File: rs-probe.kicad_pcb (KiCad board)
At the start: 4 copper layers, 40 x 14 mm, 108 parts, among them J1 USB_C_Receptacle_USB2.0, J10 Conn_01x01, J11 Conn_01x01, J2 Castellated Vias, J3 Castellated Vias, J4 Castellated Vias, J5 tag-connect-swd, J6 Conn_01x01, J7 Conn_01x01, J8 Conn_01x01, J9 Conn_01x01, Q1 NTZD3155C or CMLDM3757-TR-PBF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, SW1 EVQ-P2002W, T1 Tab, T2 Tab, U1 74LVC1T45GM,115, U10 74LVC1T45GM,115, U11 74LVC1T45GM,115, U12 NCP133AMXADJTCG, U13 NCP133AMXADJTCG, U14 NCP133AMXADJTCG, U2 74LVC1T45GM,115, U3 W25Q8, U4 NUF8401MNT4G, U5 CortexDebug, U6 RP2040, U7 NUF2042XV6T1G, U8 74LVC1T45GM,115, U9 74LVC1T45GM,115, X1 12 MHz

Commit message: Lots of work
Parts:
- removed J10, J11: Conn_01x01, connectors:pad_1.5x2.0mm
- removed J4: Castellated Vias, connectors:1x3_1.5mm_castellated
- removed TP1, TP2, TP3, TP4: TestPoint, TestPoint:TestPoint_Pad_D1.0mm
- added C31: 0.1u, passive:C_0402, F.Cu at (163.7, 90.3)
- added C32: 0.1u, passive:C_0402, F.Cu at (163.7, 87.1)
- added C33: 0.1u, passive:C_0402, F.Cu at (163.7, 88.7)
- added C34: 0.1u, passive:C_0402, F.Cu at (163.7, 83.1)
- added C35: 0.1u, passive:C_0402, F.Cu at (163.7, 84.7)
- added J1: Conn_01x01, connectors:pad_2.0x2.5mm, F.Cu at (149.9, 91.4)
- added J5: Conn_01x01, connectors:pad_2.0x2.5mm, B.Cu at (157.0, 107.0)
- J2: value Castellated Vias -> Conn_01x01; footprint connectors:1x9_1.5mm_castellated -> connectors:pad_2.0x2.5mm; moved to F.Cu
- J3: value Castellated Vias -> Conn_01x01; footprint connectors:1x2_1.5mm_castellated -> connectors:pad_2.0x2.5mm; moved to F.Cu
- J6, J7, J8, J9: footprint connectors:pad_1.5x2.0mm -> connectors:pad_2.0x2.5mm
- R10, R18, R22, R23, R24, R26: value 1Meg -> 1M
- X1: renamed from U5; value CortexDebug -> Conn_ST_STDC14
- X5: renamed from J5; value tag-connect-swd -> TagConnect
- moved J3 25.9 mm to (156.1, 91.4), turned to 0 degrees
- moved J7 22.7 mm to (166.0, 110.5)
- moved R19 21.5 mm to (173.3, 82.4), turned to 0 degrees
- moved R20 21.3 mm to (175.1, 81.8), turned to 90 degrees
- moved Q1 20.1 mm to (173.8, 81.0), turned to 90 degrees
- moved J8 19.3 mm to (163.0, 110.5)
- moved J9 19.2 mm to (160.0, 110.5)
- moved X5 17.6 mm to (169.9, 75.6)
- moved C25 16.5 mm to (165.1, 67.2)
- moved J6 15.6 mm to (154.0, 107.0)
- moved C5 14.0 mm to (158.8, 80.3), turned to 180 degrees
- moved R21 13.7 mm to (164.7, 68.6)
- moved R25 13.7 mm to (165.6, 68.6), turned to 90 degrees
- moved U12 13.7 mm to (163.2, 68.5)
- moved C24 13.7 mm to (163.2, 67.1)
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- renumbered J1 to X10, X1 to XC1
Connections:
- net /5V_KEY_EN renamed 5V_KEY_EN
- net /ADJ2_T renamed ADJ2_T
- net /ADJ_T renamed ADJ_T
- net /DIR_SWDCLK_JCLK renamed DIR_SWDCLK_JCLK
- net /DIR_SWDIO_TMS renamed DIR_SWDIO_TMS
- net /DIR_SWO_TDO renamed DIR_SWO_TDO
- net /DIR_TDI renamed DIR_TDI
- net /DIR_VCP_RX renamed DIR_VCP_RX
- net /DIR_VCP_TX renamed DIR_VCP_TX
- net /D_FS_N renamed D_FS_N
- net /D_FS_P renamed D_FS_P
- net /FUSED_5V renamed FUSED_5V
- net /GNDDetect renamed GNDDetect
- net /LED1 renamed LED1
- net /LED2 renamed LED2
- net /LED3 renamed LED3
- net /PROTECTED_5V renamed PROTECTED_5V
- net /PWM2_VS renamed PWM2_VS
- net /PWM_VS renamed PWM_VS
- net /P_SWCLK renamed P_SWCLK
- net /P_SWDIO renamed P_SWDIO
- net /SWDCLK_JCLK renamed SWDCLK_JCLK
- net /SWDIO_TMS renamed SWDIO_TMS
- net /SWO_TDO renamed SWO_TDO
- net /TDI renamed TDI
- net /TRANS_VCC renamed TRANS_VCC
- net /T_VCC_EN renamed T_VCC_EN
- net /T_VCC_MEAS renamed T_VCC_MEAS
- net /VCP_RX renamed VCP_RX
- net /VCP_TX renamed VCP_TX
- net /VS2_T renamed VS2_T
- net /VS_T renamed VS_T
- net /~{RESET} renamed ~{RESET}
- C27 pad 1: /T_VCC -> T_VCC
- D3 pad 1: /T_VCC -> T_VCC
- J2 pad 1: GND -> T_VCP_TX
- J3 pad 1: /5V_KEY -> T_VCP_RX
- J6 pad 1: GND -> 5V_KEY
- J7 pad 1: /T_VCC -> GPIO2
- J8 pad 1: /T_SWDIO_TMS -> T_VCC
- J9 pad 1: /T_SWDCLK_JCLK -> GPIO1
- Q1 pad 3: /5V_KEY -> 5V_KEY
- R10 pad 2: /T_TDI -> T_TDI
- R14 pad 2: /T_VCC -> T_VCC
- R18 pad 2: /T_VCP_RX -> T_VCP_RX
- R22 pad 2: /T_SWDIO_TMS -> T_SWDIO_TMS
- R23 pad 2: /T_SWDCLK_JCLK -> T_SWDCLK_JCLK
- R24 pad 2: /T_SWO_TDO -> T_SWO_TDO
- R26 pad 2: /T_VCP_TX -> T_VCP_TX
- R9 pad 1: /T_VCC -> T_VCC
- U4 pad 10: /T_SWDCLK_JCLK -> T_SWDCLK_JCLK
- U4 pad 11: /T_SWO_TDO -> T_SWO_TDO
- U4 pad 12: /T_TDI -> T_TDI
- U4 pad 13: /T_GNDDetect -> T_GNDDetect
- U4 pad 14: /T_~{RESET} -> T_~{RESET}
- U4 pad 15: /T_VCP_TX -> T_VCP_TX
- U4 pad 16: /T_VCP_RX -> T_VCP_RX
- U4 pad 9: /T_SWDIO_TMS -> T_SWDIO_TMS
- U6 pad 3: /GPIO1 -> GPIO1
- U6 pad 4: /GPIO2 -> GPIO2
- X1 pad 1: /T_VCC -> T_VCC
- X1 pad 10: /T_~{RESET} -> T_~{RESET}
- X1 pad 2: /T_SWDIO_TMS -> T_SWDIO_TMS
- X1 pad 4: /T_SWDCLK_JCLK -> T_SWDCLK_JCLK
- X1 pad 6: /T_SWO_TDO -> T_SWO_TDO
- X1 pad 7: /5V_KEY -> unconnected-(X1-KEY-Pad7)
- X1 pad 8: /T_TDI -> T_TDI
- X1 pad 9: /T_GNDDetect -> T_GNDDetect
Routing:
- net GND: track 99.8 -> 34.3 mm, vias 63 -> 33
- net /5V_KEY: track 51.8 -> 0.00 mm, vias 3 -> 0
- net /T_VCC: track 50.3 -> 0.00 mm, vias 4 -> 0
- net +3.3V: track 58.5 -> 21.8 mm, vias 18 -> 15
- net P_SWDIO: track 29.7 -> 0.00 mm, vias 1 -> 0
- net P_SWCLK: track 28.2 -> 0.00 mm, vias 1 -> 0
- net T_VCC_MEAS: track 27.3 -> 2.11 mm, vias 2 -> 0
- net /T_SWDIO_TMS: track 23.6 -> 0.00 mm, vias 3 -> 0
- net 5V_KEY_EN: track 24.0 -> 0.70 mm, vias 2 -> 0
- net /T_VCP_RX: track 22.0 -> 0.00 mm, vias 4 -> 0
- net /T_SWDCLK_JCLK: track 21.1 -> 0.00 mm, vias 3 -> 0
- net VS2_T: track 22.7 -> 1.60 mm, vias 2 -> 0
- net VS_T: track 19.0 -> 1.60 mm, vias 2 -> 0
- net /T_VCP_TX: track 17.3 -> 0.00 mm, vias 3 -> 0
- net /T_GNDDetect: track 16.1 -> 0.00 mm, vias 1 -> 0
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- added copper zone on B.Cu, net +3.3V
- added copper zone on F.Cu, net +3.3V
- removed copper zone on B.Cu, net GND
- removed copper zone on F.Cu, net GND

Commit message: wip
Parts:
- moved J7 35.8 mm to (154.8, 76.5)
- moved J8 35.8 mm to (151.8, 76.5)
- moved J9 35.8 mm to (148.8, 76.5)
- moved C24 16.9 mm to (171.1, 82.1)
- moved J5 16.8 mm to (150.8, 91.4), turned to 0 degrees
- moved J6 15.6 mm to (153.8, 91.4), turned to 0 degrees
- moved C25 15.5 mm to (169.4, 82.1), turned to 180 degrees
- moved U12 14.7 mm to (171.1, 80.8)
- moved R21 13.3 mm to (169.8, 80.8)
- moved R25 12.7 mm to (169.0, 80.8)
- moved X5 6.11 mm to (163.9, 76.8)
- moved R5 1.70 mm to (175.5, 92.2)
- moved R6 1.65 mm to (173.8, 92.2)
- moved C6 1.10 mm to (176.8, 90.8)
- moved R7 0.81 mm to (177.1, 92.2)
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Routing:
- net T_VCC_MEAS: track 2.11 -> 30.5 mm, vias 0 -> 2
- net DIR_VCP_TX: track 0.00 -> 14.0 mm, vias 0 -> 2
- net DIR_VCP_RX: track 0.00 -> 12.3 mm, vias 0 -> 2
- net TRANS_VCC: track 19.2 -> 7.76 mm
- net DIR_SWDCLK_JCLK: track 0.00 -> 11.0 mm, vias 0 -> 3
- net VCP_RX: track 0.00 -> 11.0 mm, vias 0 -> 2
- net VCP_TX: track 0.00 -> 10.5 mm, vias 0 -> 2
- net SWDIO_TMS: track 0.00 -> 9.68 mm, vias 0 -> 2
- net SWO_TDO: track 0.00 -> 8.99 mm, vias 0 -> 2
- net SWDCLK_JCLK: track 0.00 -> 8.58 mm, vias 0 -> 2
- net TDI: track 0.00 -> 8.56 mm, vias 0 -> 2
- net DIR_TDI: track 0.00 -> 5.48 mm, vias 0 -> 1
- net GND: track 34.3 -> 37.8 mm, vias 33 -> 36
- net Net-(D1-RK): track 2.46 -> 4.96 mm, vias 0 -> 2
- net +3.3V: track 21.8 -> 24.2 mm
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- added copper zone on B.Cu, net GND
- added copper zone on F.Cu, net GND
- removed copper zone on B.Cu, net +3.3V
- removed copper zone on F.Cu, net +3.3V

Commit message: wip
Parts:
- removed X5: TagConnect, Connector:Tag-Connect_TC2030-IDC-NL_2x03_P1.27mm_Vertical
- removed kibuzzard-61EE8014: G***, kibuzzard-61EE8014
- removed kibuzzard-61FE7ECB: G***, kibuzzard-61FE7ECB
- removed kibuzzard-61FE8065: G***, kibuzzard-61FE8065
- removed kibuzzard-61FE8092: G***, kibuzzard-61FE8092
- removed kibuzzard-61FE80B0: G***, kibuzzard-61FE80B0
- removed kibuzzard-61FE80BD: G***, kibuzzard-61FE80BD
- removed kibuzzard-6228D4B3: G***, kibuzzard-6228D4B3
- removed kibuzzard-6228D4CF: G***, kibuzzard-6228D4CF
- removed kibuzzard-63846A4C: G***, kibuzzard-63846A4C
- removed kibuzzard-6384B72D: G***, kibuzzard-6384B72D
- moved SW1 28.8 mm to (162.2, 96.9)
- moved J6 10.5 mm to (152.4, 81.0)
- moved J5 10.3 mm to (150.1, 81.1)
- moved F1 8.49 mm to (186.9, 79.9)
- moved C17 6.80 mm to (156.9, 91.0), turned to 180 degrees
- moved C19 6.79 mm to (156.9, 91.8), turned to 180 degrees
- moved FB1 6.58 mm to (183.0, 79.9), turned to 180 degrees
- moved C29 6.34 mm to (184.6, 79.9), turned to 180 degrees
- moved C16 5.20 mm to (158.6, 82.9), turned to 180 degrees
- moved C34 5.15 mm to (158.6, 83.8), turned to 180 degrees
- moved D2 5.04 mm to (181.2, 79.9)
- moved U12 4.55 mm to (175.6, 80.1)
- moved C24 4.55 mm to (175.6, 81.4)
- moved C25 4.55 mm to (173.9, 81.4)
- moved R21 4.55 mm to (174.3, 80.2)
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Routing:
- net GNDDetect: track 13.9 -> 1.20 mm
- net ~{RESET}: track 13.0 -> 1.18 mm
- net DIR_VCP_RX: track 12.3 -> 0.92 mm
- net DIR_VCP_TX: track 14.0 -> 2.92 mm
- net DIR_SWDCLK_JCLK: track 11.0 -> 1.04 mm, vias 3 -> 1
- net VCP_RX: track 11.0 -> 1.18 mm
- net SWDIO_TMS: track 9.68 -> 0.56 mm
- net SWO_TDO: track 8.99 -> 0.00 mm, vias 2 -> 0
- net SWDCLK_JCLK: track 8.58 -> 0.26 mm, vias 2 -> 1
- net TDI: track 8.56 -> 0.31 mm, vias 2 -> 1
- net VCP_TX: track 10.5 -> 3.72 mm
- net +5V: track 4.29 -> 9.82 mm, vias 3 -> 2
- net Net-(U3-DO(IO1)): track 0.00 -> 4.62 mm, vias 0 -> 2
- net P_SWCLK: track 1.12 -> 4.94 mm
- net +3.3V: track 24.2 -> 27.9 mm
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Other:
- board text removed: "By Emil Fresk @korken89"
- board text removed: "git: {GITHASH}"

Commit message: wip
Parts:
- moved SW1 21.2 mm to (169.6, 77.0)
- moved R9 11.9 mm to (159.9, 89.8), turned to -90 degrees
- moved R11 11.7 mm to (159.4, 91.5), turned to 180 degrees
- moved J6 7.48 mm to (145.1, 79.5)
- moved R12 6.15 mm to (157.4, 82.0)
- moved C21 5.66 mm to (156.2, 81.8), turned to 90 degrees
- moved R27 5.62 mm to (159.2, 82.0), turned to 0 degrees
- moved C28 5.25 mm to (161.2, 81.6)
- moved R29 5.20 mm to (160.4, 81.6)
- moved J5 5.17 mm to (145.1, 82.2)
- moved C27 4.52 mm to (149.5, 80.8)
- moved C5 4.52 mm to (154.1, 80.4)
- moved D3 4.52 mm to (150.7, 82.2)
- moved R1 4.52 mm to (155.7, 80.4)
- moved R14 4.52 mm to (152.4, 82.2)
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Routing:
- net GND: track 41.5 -> 20.1 mm, vias 38 -> 42
- net T_VCC_MEAS: track 32.4 -> 14.1 mm, vias 2 -> 3
- net TRANS_VCC: track 11.2 -> 4.64 mm
- net T_VCC: track 10.0 -> 4.58 mm
- net 5V_KEY_EN: track 5.92 -> 0.84 mm
- net Net-(U1-B): track 3.61 -> 0.00 mm
- net +3.3V: track 27.9 -> 24.5 mm
- net VCP_TX: track 3.72 -> 0.64 mm
- net T_VCP_RX: track 8.15 -> 5.18 mm
- net DIR_TDI: track 2.59 -> 0.00 mm
- net Net-(U2-B): track 2.16 -> 0.00 mm
- net DIR_VCP_TX: track 2.92 -> 0.90 mm
- net ADJ2_T: track 3.17 -> 1.31 mm
- net VS2_T: track 1.60 -> 0.00 mm
- net Net-(D1-RK): track 4.96 -> 3.59 mm
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
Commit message: wip
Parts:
- added X5: TagConnect, Connector:Tag-Connect_TC2030-IDC-NL_2x03_P1.27mm_Vertical, F.Cu at (166.5, 75.4)
- SW1: footprint Button_Switch_SMD:SW_SPST_EVQP2 -> pushbuttons:PCB_JumperButton; moved to B.Cu
- moved SW1 18.3 mm to (186.6, 84.0), turned to 180 degrees
- moved R9 3.56 mm to (156.9, 91.8), turned to 0 degrees
- moved C19 3.28 mm to (159.7, 90.0), turned to 90 degrees
- moved R11 1.33 mm to (158.2, 91.8), turned to 90 degrees
- moved C20 0.32 mm to (163.4, 88.8)
- moved C31 0.32 mm to (163.4, 89.6)
- moved C18 0.16 mm to (163.4, 87.0)
- moved C33 0.16 mm to (163.4, 87.8)
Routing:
- net T_VCC: track 4.58 -> 19.0 mm, vias 0 -> 2
- net VCP_RX: track 1.28 -> 14.3 mm
- net VCP_TX: track 0.64 -> 11.8 mm
- net Net-(R2-Pad2): track 0.00 -> 8.02 mm, vias 0 -> 1
- net DIR_SWDCLK_JCLK: track 1.04 -> 6.89 mm, vias 1 -> 2
- net GND: track 20.1 -> 25.0 mm
- net SWDCLK_JCLK: track 0.26 -> 4.99 mm, vias 1 -> 2
- net DIR_VCP_RX: track 0.61 -> 5.26 mm
- net TDI: track 0.00 -> 4.21 mm
- net P_SWCLK: track 4.31 -> 0.44 mm, vias 1 -> 0
- net T_VCC_MEAS: track 14.1 -> 17.8 mm, vias 3 -> 0
- net +3.3V: track 24.5 -> 20.8 mm
- net TRANS_VCC: track 4.64 -> 8.03 mm, vias 5 -> 8
- net DIR_TDI: track 0.00 -> 2.84 mm
- net P_SWDIO: track 2.93 -> 0.32 mm, vias 1 -> 0
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- removed copper zone on In2.Cu, net GND

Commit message: wip
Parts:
- removed X5: TagConnect, Connector:Tag-Connect_TC2030-IDC-NL_2x03_P1.27mm_Vertical
- J5, J6, J7, J8, J9: moved to F.Cu
- moved J6 28.5 mm to (173.6, 80.5), turned to 180 degrees
- moved J9 20.4 mm to (168.8, 80.5), turned to 0 degrees
- moved J8 19.8 mm to (171.2, 80.5), turned to 0 degrees
- moved J5 19.0 mm to (164.0, 80.5), turned to 180 degrees
- moved J7 12.3 mm to (166.4, 80.5), turned to 0 degrees
- moved R25 3.56 mm to (175.5, 83.1), turned to 0 degrees
- moved C25 2.55 mm to (176.4, 81.9), turned to -90 degrees
- moved C24 2.19 mm to (177.7, 81.9), turned to -90 degrees
- moved R21 2.18 mm to (175.6, 81.9), turned to 90 degrees
- moved U12 0.88 mm to (176.5, 80.2)
- moved R28 0.54 mm to (162.1, 80.8), turned to -90 degrees
- moved R17 0.21 mm to (166.9, 83.1)
- moved R4 0.20 mm to (185.1, 91.8)
- moved J2 0.20 mm to (152.4, 91.5)
- moved J1 0.20 mm to (149.9, 91.6)
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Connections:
- U6 pad 11: GNDDetect -> unconnected-(U6-GPIO8-Pad11)
- U6 pad 12: ~{RESET} -> unconnected-(U6-GPIO9-Pad12)
- U6 pad 16: unconnected-(U6-GPIO13-Pad16) -> DIR_SWDCLK_JCLK
- U6 pad 17: unconnected-(U6-GPIO14-Pad17) -> GNDDetect
- U6 pad 18: unconnected-(U6-GPIO15-Pad18) -> ~{RESET}
- U6 pad 29: unconnected-(U6-GPIO18-Pad29) -> DIR_TDI
- U6 pad 30: DIR_SWDCLK_JCLK -> DIR_VCP_TX
- U6 pad 35: DIR_TDI -> unconnected-(U6-GPIO23-Pad35)
- U6 pad 36: DIR_VCP_TX -> unconnected-(U6-GPIO24-Pad36)
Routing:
- net FUSED_5V: track 10.2 -> 80.3 mm, vias 0 -> 5
- net TRANS_VCC: track 8.03 -> 33.1 mm
- net T_VCC: track 19.0 -> 43.8 mm, vias 2 -> 3
- net T_VCC_EN: track 0.00 -> 24.0 mm
- net PWM_VS: track 0.00 -> 20.4 mm, vias 0 -> 2
- net ~{RESET}: track 0.64 -> 20.4 mm
- net GNDDetect: track 0.00 -> 18.8 mm, vias 1 -> 2
- net PWM2_VS: track 0.00 -> 11.6 mm, vias 0 -> 2
- net SWO_TDO: track 0.00 -> 11.4 mm, vias 1 -> 2
- net DIR_SWO_TDO: track 0.00 -> 11.3 mm, vias 1 -> 2
- net DIR_VCP_RX: track 5.26 -> 15.9 mm
- net DIR_SWDIO_TMS: track 0.00 -> 9.60 mm
- net SWDIO_TMS: track 0.56 -> 9.89 mm
- net GPIO2: track 0.00 -> 8.66 mm
- net +5V: track 8.77 -> 0.24 mm, vias 2 -> 4
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- added copper zone on F.Cu, net +3.3V
- added copper zone on In2.Cu, net +5V

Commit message: clearing drc errors
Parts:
- D1: value LTST-C19HE1WT -> 7
- U13, U14: footprint Package_DFN_QFN:DFN-6-1EP_1.2x1.2mm_P0.4mm_EP0.3x0.94mm_PullBack -> dfn:DFN-6-1EP_1.2x1.2mm_P0.4mm_EP0.3x0.94mm_PullBack
- moved J3 1.20 mm to (154.9, 91.5)

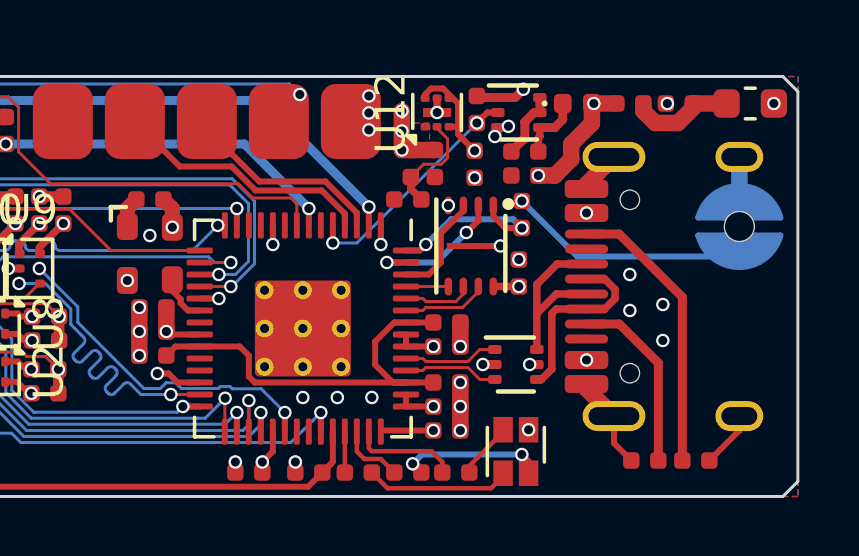
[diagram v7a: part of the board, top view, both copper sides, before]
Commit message: fixing missing 3D models
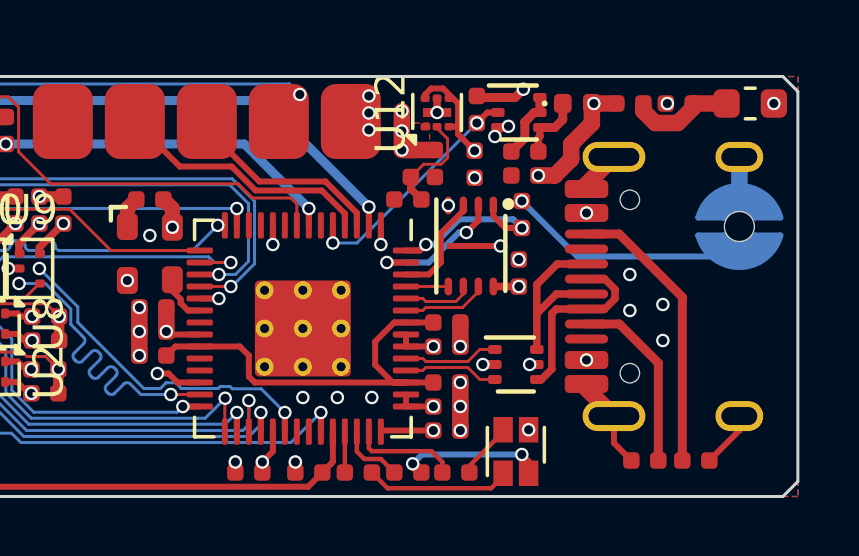
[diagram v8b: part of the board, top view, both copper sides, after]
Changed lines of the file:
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@@
 			(pintype "passive")
 		)
-		(model "${KICAD8_3DMODEL_DIR}/Diode_SMD.3dshapes/D_0402_1005Metric.wrl"
+		(model "${KIPRJMOD}/kicad_libs/3dmodels/step/SMD1006_step/3D_Model_SMD1006_Rev.0.stp"
 			(offset
 				(xyz 0 0 0)
@@
 			)
 			(rotate
-				(xyz 0 0 0)
+				(xyz 0 0 90)
 			)
 		)
@@
 			(pintype "passive")
 		)
-		(model "${KICAD8_3DMODEL_DIR}/LED_SMD.3dshapes/LED_LiteOn_LTST-C19HE1WT.wrl"
+		(model "${KIPRJMOD}/kicad_libs/3dmodels/step/LTST_C19HE1WT/LTST-C19HE1WT.step"
 			(offset
 				(xyz 0 0 0)
@@
 			)
 			(rotate
-				(xyz 0 0 0)
+				(xyz -90 0 90)
 			)
 		)
@@
 		)
 		(property "Value" "W25Q8"
-			(at 0 1.35 -90)
+			(at 0 1.35 90)
 			(layer "F.Fab")
 			(effects
@@
 		)
 		(property "Footprint" "son:USON-8-3x2mm-EP"
-			(at 0 0 -90)
+			(at 0 0 90)
 			(layer "F.Fab")
 			(hide yes)
@@
 		)
 		(property "Datasheet" ""
-			(at 0 0 -90)
+			(at 0 0 90)
 			(layer "F.Fab")
 			(hide yes)
@@
 		)
 		(property "Description" ""
-			(at 0 0 -90)
+			(at 0 0 90)
 			(layer "F.Fab")
 			(hide yes)
@@
 			)
 		)
-		(property "LCSC" "C2063555, C2759920, C2983691, C559220, C394861"
+		(property "LCSC" "C2983691, C401667, C2759920"
 			(at 92.9 262.3 0)
 			(layer "F.Fab")
@@
 		)
 		(fp_text user "${REFERENCE}"
-			(at 0 0 -90)
+			(at 0 0 90)
 			(layer "F.Fab")
 			(effects
@@
 			(pintype "passive")
 		)
+		(model "${KIPRJMOD}/kicad_libs/3dmodels/step/USON_3X2_WIN.step"
+			(offset
+				(xyz 0 0 0)
+			)
+			(scale
+				(xyz 1 1 1)
+			)
+			(rotate
+				(xyz 0 0 0)
+			)
+		)
 	)
 	(footprint "passive:R_0402"
@@
 			(pintype "passive")
 		)
-		(model "${KICAD8_3DMODEL_DIR}/Diode_SMD.3dshapes/D_0402_1005Metric.wrl"
+		(model "${KIPRJMOD}/kicad_libs/3dmodels/step/SMD1006_step/3D_Model_SMD1006_Rev.0.stp"
 			(offset
 				(xyz 0 0 0)
@@
 			)
 			(rotate
-				(xyz 0 0 0)
+				(xyz 0 0 90)
 			)
 		)
@@
 			(zone_connect 2)
 		)
-		(model "${KICAD8_3DMODEL_DIR}/Package_DFN_QFN.3dshapes/DFN-6-1EP_1.2x1.2mm_P0.4mm_EP0.3x0.94mm_PullBack.wrl"
+		(model "${KICAD8_3DMODEL_DIR}/Package_DFN_QFN.3dshapes/DFN-6-1EP_1.2x1.2mm_P0.4mm_EP0.3x0.94mm.wrl"
 			(offset
 				(xyz 0 0 0)
@@
 	)
 	(segment
-		(start 179.01 83.76)
-		(end 176.94 83.76)
+		(start 176.375736 84.6)
+		(end 176.1 84.6)
 		(width 0.2)
 		(layer "B.Cu")
@@
 	)
 	(segment
-		(start 176.94 83.76)
-		(end 176.1 84.6)
+		(start 179.3 84.05)
+		(end 179.01 83.76)
 		(width 0.2)
 		(layer "B.Cu")
@@
 	)
 	(segment
-		(start 179.3 84.05)
-		(end 179.01 83.76)
+		(start 177.215736 83.76)
+		(end 176.375736 84.6)
+		(width 0.2)
+		(layer "B.Cu")
+		(net 50)
+	)
+	(segment
+		(start 179.01 83.76)
+		(end 177.215736 83.76)
 		(width 0.2)
 		(layer "B.Cu")
@@
 	)
 	(segment
-		(start 176.45 85.2)
+		(start 176.2 85.2)
 		(end 174.8 85.2)
 		(width 0.2)
@@
 	)
 	(segment
+		(start 177.2 84.2)
+		(end 176.2 85.2)
+		(width 0.2)
+		(layer "B.Cu")
+		(net 65)
+	)
+	(segment
 		(start 177.45 84.2)
-		(end 176.45 85.2)
+		(end 177.2 84.2)
 		(width 0.2)
 		(layer "B.Cu")
